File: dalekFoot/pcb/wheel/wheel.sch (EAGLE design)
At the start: 81 parts, among them IC1 LM1117MP-3.3, IC2 LM1117MP-3.3, IC3 LM1117MP-3.3, IC4 4051D, IC5 4051D, IC6 LM1117MP-3.3, U1 TB6612FNG(O,C,8,EL, U2 SS8050-SOT-23, U3 SS8050-SOT-23, U4 SS8050-SOT-23, U5 TB6612FNG(O,C,8,EL, U6 TB6612FNG(O,C,8,EL

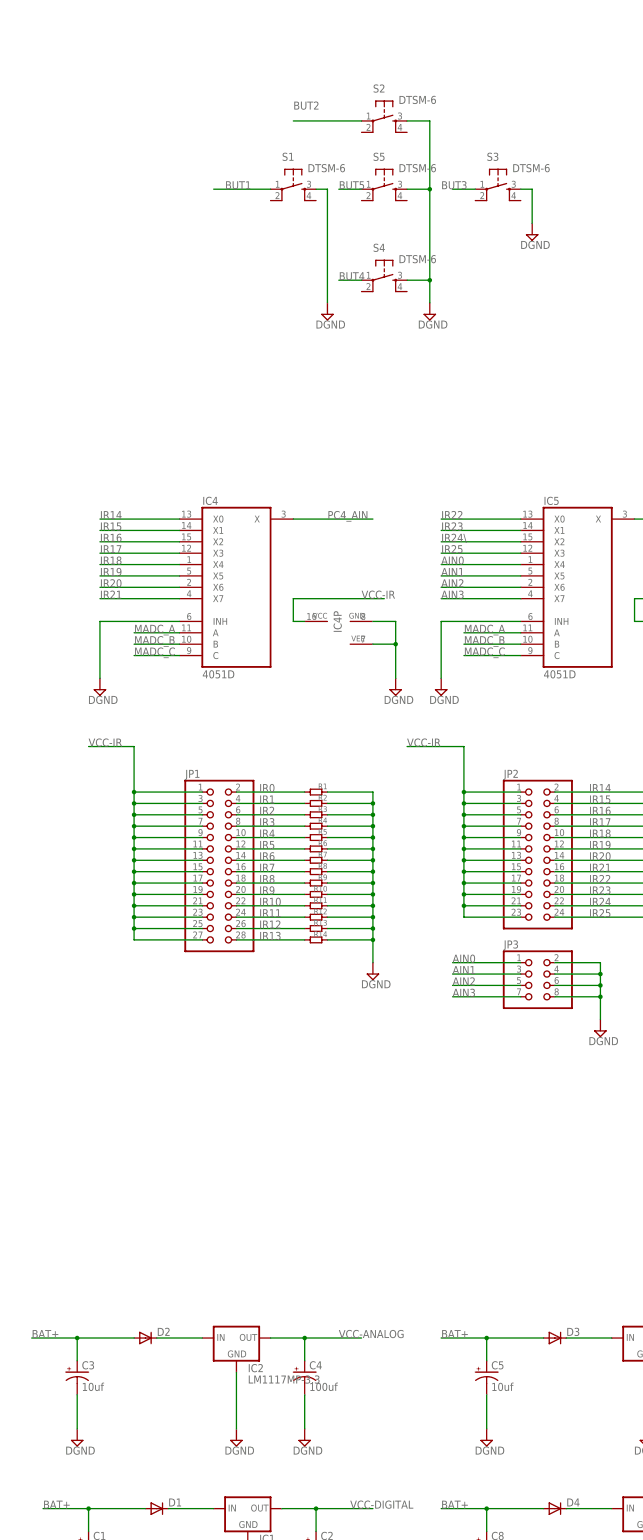
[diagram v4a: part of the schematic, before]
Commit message: 1. bugfix: fix net name typo 2. remove one unused phase power supply 3. make board more compact
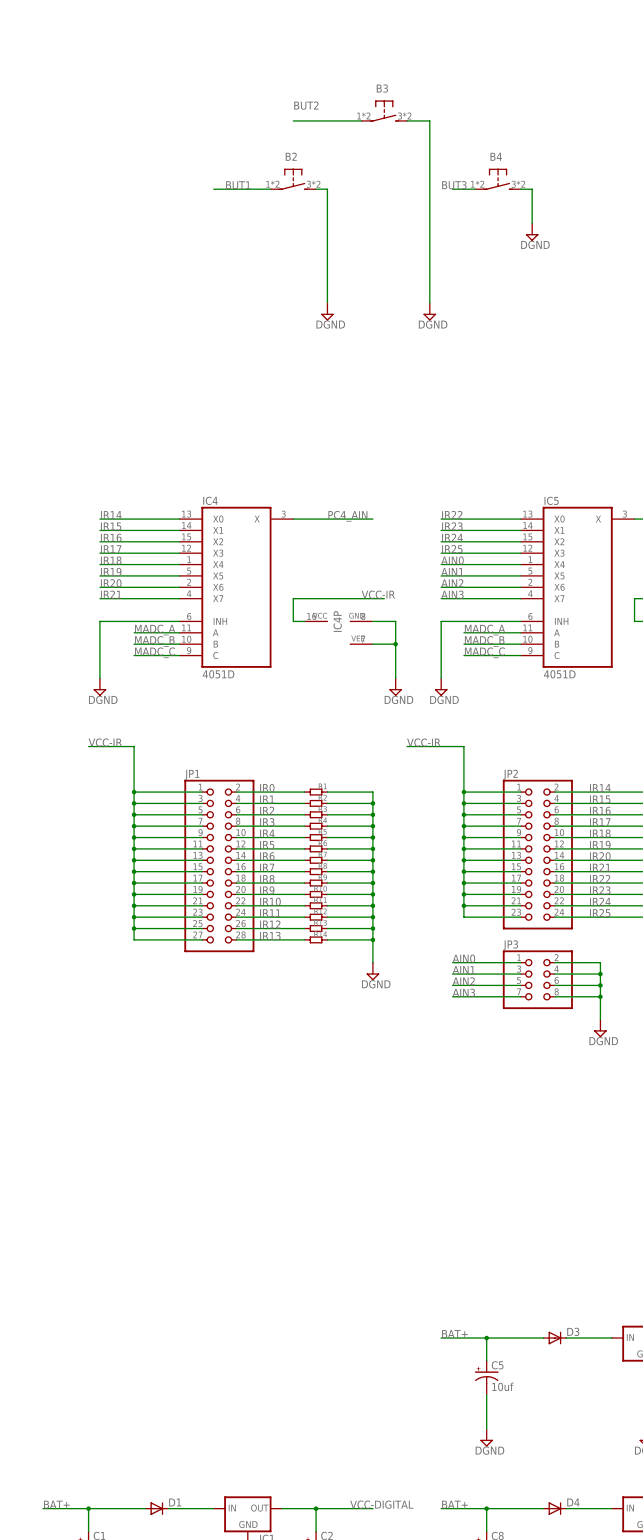
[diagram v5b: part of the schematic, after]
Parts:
- removed C3: 10uf, rcl:CPOL-US153CLV-0505
- removed C4: 100uf, rcl:CPOL-US153CLV-0605
- removed D2: (no value), diode:DIODE-DO-214AC
- removed IC2: LM1117MP-3.3, lm1117:LM1117MP-3.3
- removed S1, S2, S3, S4, S5: DTSM-6, switch-tact:DTSM-6
- added B2, B3, B4: (no value), switch-tact:DTSM-6-2PIN
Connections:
- removed net IR24\: IC5A.X2
- removed net N$1: D2.C, IC2.IN
- removed net VCC-ANALOG: C4.+, IC2.OUT
- net BAT+: no longer C3.+, D2.A
- net BUT1: now also B2.1; no longer S1.1
- net BUT2: now also B3.1; no longer S2.1
- net BUT3: now also B4.1; no longer S3.1
- net BUT4: no longer S4.1
- net BUT5: no longer S5.1
- net DGND: now also B2.2, B3.2, B4.2; no longer C3.-, C4.-, IC2.GND, S1.3, S2.3, S3.3, S4.3, S5.3
- net IR24: now also IC5A.X2
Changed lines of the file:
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@@
 <part name="SUPPLY2" library="supply2" deviceset="DGND" device=""/>
 <part name="SUPPLY3" library="supply2" deviceset="DGND" device=""/>
-<part name="IC2" library="lm1117" deviceset="LM1117?-*" device="MP" technology="3.3"/>
-<part name="SUPPLY4" library="supply2" deviceset="DGND" device=""/>
-<part name="C3" library="rcl" deviceset="CPOL-US" device="153CLV-0505" value="10uf"/>
-<part name="C4" library="rcl" deviceset="CPOL-US" device="153CLV-0605" value="100uf"/>
-<part name="SUPPLY5" library="supply2" deviceset="DGND" device=""/>
-<part name="SUPPLY6" library="supply2" deviceset="DGND" device=""/>
 <part name="U1" library="TB6612FNG" deviceset="TB6612FNG(O,C,8,EL" device=""/>
 <part name="SUPPLY7" library="supply2" deviceset="DGND" device=""/>
@@
 <part name="SUPPLY8" library="supply2" deviceset="DGND" device=""/>
 <part name="D1" library="diode" deviceset="DIODE-" device="DO-214AC"/>
-<part name="D2" library="diode" deviceset="DIODE-" device="DO-214AC"/>
 <part name="R1" library="hqc" deviceset="R-0603" device=""/>
 <part name="R2" library="hqc" deviceset="R-0603" device=""/>
@@
 <part name="SUPPLY39" library="supply2" deviceset="DGND" device=""/>
 <part name="R36" library="rcl" deviceset="R-EU_" device="R0402"/>
-<part name="S1" library="switch-tact" deviceset="DTSM-6" device=""/>
-<part name="S2" library="switch-tact" deviceset="DTSM-6" device=""/>
-<part name="S3" library="switch-tact" deviceset="DTSM-6" device=""/>
-<part name="S4" library="switch-tact" deviceset="DTSM-6" device=""/>
-<part name="S5" library="switch-tact" deviceset="DTSM-6" device=""/>
+<part name="B2" library="switch-tact" deviceset="DTSM-6-2PIN" device=""/>
+<part name="B3" library="switch-tact" deviceset="DTSM-6-2PIN" device=""/>
+<part name="B4" library="switch-tact" deviceset="DTSM-6-2PIN" device=""/>
 </parts>
 <sheets>
@@
 <instance part="SUPPLY2" gate="G$1" x="81.28" y="58.42"/>
 <instance part="SUPPLY3" gate="G$1" x="30.48" y="58.42"/>
-<instance part="IC2" gate="G$1" x="63.5" y="119.38"/>
-<instance part="SUPPLY4" gate="G$1" x="63.5" y="96.52"/>
-<instance part="C3" gate="G$1" x="27.94" y="111.76"/>
-<instance part="C4" gate="G$1" x="78.74" y="111.76"/>
-<instance part="SUPPLY5" gate="G$1" x="78.74" y="96.52"/>
-<instance part="SUPPLY6" gate="G$1" x="27.94" y="96.52"/>
 <instance part="U1" gate="G$1" x="53.34" y="596.9"/>
 <instance part="SUPPLY7" gate="G$1" x="73.66" y="558.8"/>
@@
 <instance part="SUPPLY8" gate="G$1" x="330.2" y="43.18"/>
 <instance part="D1" gate="G$1" x="45.72" y="81.28"/>
-<instance part="D2" gate="G$1" x="43.18" y="119.38"/>
 <instance part="R1" gate="G$1" x="81.28" y="241.3" rot="R180"/>
 <instance part="R2" gate="G$1" x="81.28" y="238.76" rot="R180"/>
@@
 <instance part="SUPPLY39" gate="G$1" x="325.12" y="215.9"/>
 <instance part="R36" gate="G$1" x="312.42" y="228.6"/>
-<instance part="S1" gate="G$1" x="76.2" y="375.92" rot="R270"/>
-<instance part="S2" gate="G$1" x="96.52" y="391.16" rot="R270"/>
-<instance part="S3" gate="G$1" x="121.92" y="375.92" rot="R270"/>
-<instance part="S4" gate="G$1" x="96.52" y="355.6" rot="R270"/>
-<instance part="S5" gate="G$1" x="96.52" y="375.92" rot="R270"/>
+<instance part="B2" gate="G$1" x="76.2" y="375.92" rot="R270"/>
+<instance part="B3" gate="G$1" x="96.52" y="391.16" rot="R270"/>
+<instance part="B4" gate="G$1" x="121.92" y="375.92" rot="R270"/>
 </instances>
 <busses>
@@
 <pinref part="SUPPLY2" gate="G$1" pin="DGND"/>
 <wire x1="81.28" y1="68.58" x2="81.28" y2="60.96" width="0.1524" layer="91"/>
-</segment>
-<segment>
-<pinref part="IC2" gate="G$1" pin="GND"/>
-<pinref part="SUPPLY4" gate="G$1" pin="DGND"/>
-<wire x1="63.5" y1="111.76" x2="63.5" y2="99.06" width="0.1524" layer="91"/>
-</segment>
-<segment>
-<pinref part="SUPPLY6" gate="G$1" pin="DGND"/>
-<pinref part="C3" gate="G$1" pin="-"/>
-<wire x1="27.94" y1="99.06" x2="27.94" y2="106.68" width="0.1524" layer="91"/>
-</segment>
-<segment>
-<pinref part="C4" gate="G$1" pin="-"/>
-<pinref part="SUPPLY5" gate="G$1" pin="DGND"/>
-<wire x1="78.74" y1="106.68" x2="78.74" y2="99.06" width="0.1524" layer="91"/>
 </segment>
 <segment>
@@
 </segment>
 <segment>
-<wire x1="101.6" y1="355.6" x2="106.68" y2="355.6" width="0.1524" layer="91"/>
 <pinref part="SUPPLY31" gate="G$1" pin="DGND"/>
-<wire x1="106.68" y1="355.6" x2="106.68" y2="350.52" width="0.1524" layer="91"/>
-<wire x1="101.6" y1="375.92" x2="106.68" y2="375.92" width="0.1524" layer="91"/>
-<wire x1="106.68" y1="375.92" x2="106.68" y2="355.6" width="0.1524" layer="91"/>
-<junction x="106.68" y="355.6"/>
+<wire x1="106.68" y1="391.16" x2="106.68" y2="350.52" width="0.1524" layer="91"/>
 <wire x1="101.6" y1="391.16" x2="106.68" y2="391.16" width="0.1524" layer="91"/>
-<wire x1="106.68" y1="391.16" x2="106.68" y2="375.92" width="0.1524" layer="91"/>
-<junction x="106.68" y="375.92"/>
-<pinref part="S2" gate="G$1" pin="3"/>
-<pinref part="S5" gate="G$1" pin="3"/>
-<pinref part="S4" gate="G$1" pin="3"/>
+<pinref part="B3" gate="G$1" pin="2"/>
 </segment>
 <segment>
@@
 <wire x1="83.82" y1="375.92" x2="83.82" y2="350.52" width="0.1524" layer="91"/>
 <pinref part="SUPPLY32" gate="G$1" pin="DGND"/>
-<pinref part="S1" gate="G$1" pin="3"/>
+<pinref part="B2" gate="G$1" pin="2"/>
 </segment>
 <segment>
@@
 <wire x1="129.54" y1="375.92" x2="129.54" y2="368.3" width="0.1524" layer="91"/>
 <pinref part="SUPPLY33" gate="G$1" pin="DGND"/>
-<pinref part="S3" gate="G$1" pin="3"/>
+<pinref part="B4" gate="G$1" pin="2"/>
 </segment>
 <segment>
@@
 </segment>
 <segment>
-<wire x1="17.78" y1="119.38" x2="27.94" y2="119.38" width="0.1524" layer="91"/>
-<pinref part="C3" gate="G$1" pin="+"/>
-<wire x1="27.94" y1="114.3" x2="27.94" y2="119.38" width="0.1524" layer="91"/>
-<label x="17.78" y="119.38" size="1.778" layer="95"/>
-<wire x1="27.94" y1="119.38" x2="40.64" y2="119.38" width="0.1524" layer="91"/>
-<junction x="27.94" y="119.38"/>
-<pinref part="D2" gate="G$1" pin="A"/>
-</segment>
-<segment>
 <pinref part="U1" gate="G$1" pin="VM1"/>
 <wire x1="68.58" y1="619.76" x2="73.66" y2="619.76" width="0.1524" layer="91"/>
@@
 </segment>
 </net>
-<net name="VCC-ANALOG" class="0">
-<segment>
-<pinref part="IC2" gate="G$1" pin="OUT"/>
-<wire x1="71.12" y1="119.38" x2="78.74" y2="119.38" width="0.1524" layer="91"/>
-<pinref part="C4" gate="G$1" pin="+"/>
-<wire x1="78.74" y1="119.38" x2="91.44" y2="119.38" width="0.1524" layer="91"/>
-<wire x1="78.74" y1="114.3" x2="78.74" y2="119.38" width="0.1524" layer="91"/>
-<junction x="78.74" y="119.38"/>
-<label x="86.36" y="119.38" size="1.778" layer="95"/>
-</segment>
-</net>
 <net name="AO3.1" class="0">
 <segment>
@@
 </segment>
 </net>
-<net name="N$1" class="0">
-<segment>
-<pinref part="D2" gate="G$1" pin="C"/>
-<pinref part="IC2" gate="G$1" pin="IN"/>
-<wire x1="45.72" y1="119.38" x2="55.88" y2="119.38" width="0.1524" layer="91"/>
-</segment>
-</net>
 <net name="N$5" class="0">
 <segment>
@@
 <wire x1="154.94" y1="215.9" x2="134.62" y2="215.9" width="0.1524" layer="91"/>
 <label x="142.24" y="215.9" size="1.778" layer="95"/>
+</segment>
+<segment>
+<pinref part="IC5" gate="A" pin="X2"/>
+<wire x1="127" y1="297.18" x2="109.22" y2="297.18" width="0.1524" layer="91"/>
+<label x="109.22" y="297.18" size="1.778" layer="95"/>
 </segment>
 </net>
@@
 </segment>
 </net>
-<net name="IR24\" class="0">
-<segment>
-<pinref part="IC5" gate="A" pin="X2"/>
-<wire x1="127" y1="297.18" x2="109.22" y2="297.18" width="0.1524" layer="91"/>
-<label x="109.22" y="297.18" size="1.778" layer="95"/>
-</segment>
-</net>
 <net name="MADC_A" class="0">
 <segment>
@@
 <wire x1="71.12" y1="375.92" x2="58.42" y2="375.92" width="0.1524" layer="91"/>
 <label x="60.96" y="375.92" size="1.778" layer="95"/>
-<pinref part="S1" gate="G$1" pin="1"/>
+<pinref part="B2" gate="G$1" pin="1"/>
 </segment>
 </net>
@@
 <wire x1="91.44" y1="391.16" x2="76.2" y2="391.16" width="0.1524" layer="91"/>
 <label x="76.2" y="393.7" size="1.778" layer="95"/>
-<pinref part="S2" gate="G$1" pin="1"/>
+<pinref part="B3" gate="G$1" pin="1"/>
 </segment>
 </net>
@@
 <wire x1="111.76" y1="375.92" x2="116.84" y2="375.92" width="0.1524" layer="91"/>
 <label x="109.22" y="375.92" size="1.778" layer="95"/>
-<pinref part="S3" gate="G$1" pin="1"/>
+<pinref part="B4" gate="G$1" pin="1"/>
 </segment>
 </net>
@@
 <label x="378.46" y="96.52" size="1.778" layer="95"/>
 </segment>
-<segment>
-<wire x1="86.36" y1="355.6" x2="91.44" y2="355.6" width="0.1524" layer="91"/>
-<label x="86.36" y="355.6" size="1.778" layer="95"/>
-<pinref part="S4" gate="G$1" pin="1"/>
-</segment>
 </net>
 <net name="BUT5" class="0">
@@
 <label x="378.46" y="93.98" size="1.778" layer="95"/>
 </segment>
-<segment>
-<wire x1="91.44" y1="375.92" x2="86.36" y2="375.92" width="0.1524" layer="91"/>
-<label x="86.36" y="375.92" size="1.778" layer="95"/>
-<pinref part="S5" gate="G$1" pin="1"/>
-</segment>
-</net>
+</net>

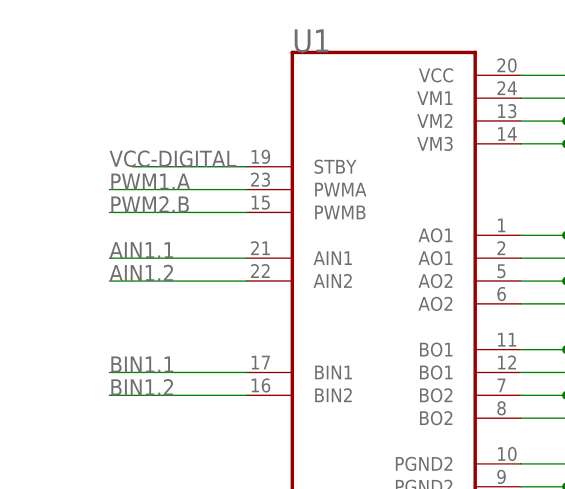
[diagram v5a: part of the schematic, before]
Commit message: modify u1 bug and IRT
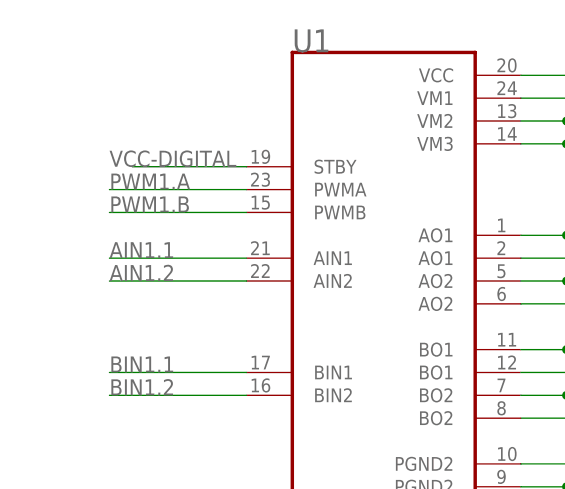
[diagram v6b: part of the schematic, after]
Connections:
- net PWM1.B: now also U1.PWMB
- net PWM2.B: no longer U1.PWMB
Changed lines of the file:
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@@
 <?xml version="1.0" encoding="utf-8"?>
 <!DOCTYPE eagle SYSTEM "eagle.dtd">
-<eagle version="7.2.0">
+<eagle version="8.2.1">
 <drawing>
 <settings>
@@
 <setting verticaltext="up"/>
 </settings>
-<grid distance="0.1" unitdist="inch" unit="mil" style="lines" multiple="1" display="yes" altdistance="0.01" altunitdist="inch" altunit="inch"/>
+<grid distance="0.1" unitdist="inch" unit="inch" style="lines" multiple="1" display="no" altdistance="0.01" altunitdist="inch" altunit="inch"/>
 <layers>
 <layer number="1" name="Top" color="4" fill="1" visible="no" active="no"/>
@@
 </segment>
 <segment>
+<pinref part="U5" gate="G$1" pin="PWMB"/>
+<wire x1="129.54" y1="607.06" x2="144.78" y2="607.06" width="0.1524" layer="91"/>
+<label x="129.54" y="607.06" size="1.778" layer="95"/>
+</segment>
+</net>
+<net name="LED1" class="0">
+<segment>
+<pinref part="U$1" gate="G$1" pin="P$C6"/>
+<wire x1="330.2" y1="88.9" x2="337.82" y2="88.9" width="0.1524" layer="91"/>
+<label x="332.74" y="88.9" size="1.778" layer="95"/>
+</segment>
+<segment>
+<pinref part="R30" gate="G$1" pin="P$1"/>
+<wire x1="83.82" y1="431.8" x2="71.12" y2="431.8" width="0.1524" layer="91"/>
+<label x="71.12" y="431.8" size="1.778" layer="95"/>
+</segment>
+</net>
+<net name="LED2" class="0">
+<segment>
+<pinref part="U$1" gate="G$1" pin="P$C7"/>
+<wire x1="330.2" y1="86.36" x2="337.82" y2="86.36" width="0.1524" layer="91"/>
+<label x="332.74" y="86.36" size="1.778" layer="95"/>
+</segment>
+<segment>
+<pinref part="R31" gate="G$1" pin="P$1"/>
+<wire x1="134.62" y1="431.8" x2="121.92" y2="431.8" width="0.1524" layer="91"/>
+<label x="124.46" y="431.8" size="1.778" layer="95"/>
+</segment>
+</net>
+<net name="PWM3.A" class="0">
+<segment>
+<pinref part="U$1" gate="G$1" pin="P$C8"/>
+<wire x1="330.2" y1="83.82" x2="337.82" y2="83.82" width="0.1524" layer="91"/>
+<label x="332.74" y="83.82" size="1.778" layer="95"/>
+</segment>
+<segment>
+<pinref part="U6" gate="G$1" pin="PWMA"/>
+<wire x1="266.7" y1="609.6" x2="251.46" y2="609.6" width="0.1524" layer="91"/>
+<label x="251.46" y="609.6" size="1.778" layer="95"/>
+</segment>
+</net>
+<net name="PWM3.B" class="0">
+<segment>
+<pinref part="U6" gate="G$1" pin="PWMB"/>
+<wire x1="251.46" y1="607.06" x2="266.7" y2="607.06" width="0.1524" layer="91"/>
+<label x="251.46" y="607.06" size="1.778" layer="95"/>
+</segment>
+<segment>
+<pinref part="U$1" gate="G$1" pin="P$A15"/>
+<wire x1="281.94" y1="66.04" x2="292.1" y2="66.04" width="0.1524" layer="91"/>
+<label x="284.48" y="66.04" size="1.778" layer="95"/>
+</segment>
+</net>
+<net name="N$9" class="0">
+<segment>
+<pinref part="R29" gate="G$1" pin="P$2"/>
+<pinref part="C7" gate="G$1" pin="P$1"/>
+<wire x1="25.4" y1="431.8" x2="30.48" y2="431.8" width="0.1524" layer="91"/>
+</segment>
+</net>
+<net name="N$12" class="0">
+<segment>
+<pinref part="C7" gate="G$1" pin="P$2"/>
+<pinref part="U2" gate="G$1" pin="P$B"/>
+<wire x1="35.56" y1="431.8" x2="40.64" y2="431.8" width="0.1524" layer="91"/>
+</segment>
+</net>
+<net name="PWM1.A" class="0">
+<segment>
+<pinref part="U$1" gate="G$1" pin="P$D12"/>
+<wire x1="353.06" y1="73.66" x2="360.68" y2="73.66" width="0.1524" layer="91"/>
+<label x="355.6" y="73.66" size="1.778" layer="95"/>
+</segment>
+<segment>
+<pinref part="U1" gate="G$1" pin="PWMA"/>
+<wire x1="38.1" y1="609.6" x2="22.86" y2="609.6" width="0.1524" layer="91"/>
+<label x="22.86" y="609.6" size="1.778" layer="95"/>
+</segment>
+</net>
+<net name="PWM1.B" class="0">
+<segment>
+<pinref part="U$1" gate="G$1" pin="P$D13"/>
+<wire x1="360.68" y1="71.12" x2="353.06" y2="71.12" width="0.1524" layer="91"/>
+<label x="355.6" y="71.12" size="1.778" layer="95"/>
+</segment>
+<segment>
 <pinref part="U1" gate="G$1" pin="PWMB"/>
 <wire x1="22.86" y1="607.06" x2="38.1" y2="607.06" width="0.1524" layer="91"/>
 <label x="22.86" y="607.06" size="1.778" layer="95"/>
 </segment>
-<segment>
-<pinref part="U5" gate="G$1" pin="PWMB"/>
-<wire x1="129.54" y1="607.06" x2="144.78" y2="607.06" width="0.1524" layer="91"/>
-<label x="129.54" y="607.06" size="1.778" layer="95"/>
-</segment>
-</net>
-<net name="LED1" class="0">
-<segment>
-<pinref part="U$1" gate="G$1" pin="P$C6"/>
-<wire x1="330.2" y1="88.9" x2="337.82" y2="88.9" width="0.1524" layer="91"/>
-<label x="332.74" y="88.9" size="1.778" layer="95"/>
-</segment>
-<segment>
-<pinref part="R30" gate="G$1" pin="P$1"/>
-<wire x1="83.82" y1="431.8" x2="71.12" y2="431.8" width="0.1524" layer="91"/>
-<label x="71.12" y="431.8" size="1.778" layer="95"/>
-</segment>
-</net>
-<net name="LED2" class="0">
-<segment>
-<pinref part="U$1" gate="G$1" pin="P$C7"/>
-<wire x1="330.2" y1="86.36" x2="337.82" y2="86.36" width="0.1524" layer="91"/>
-<label x="332.74" y="86.36" size="1.778" layer="95"/>
-</segment>
-<segment>
-<pinref part="R31" gate="G$1" pin="P$1"/>
-<wire x1="134.62" y1="431.8" x2="121.92" y2="431.8" width="0.1524" layer="91"/>
-<label x="124.46" y="431.8" size="1.778" layer="95"/>
-</segment>
-</net>
-<net name="PWM3.A" class="0">
-<segment>
-<pinref part="U$1" gate="G$1" pin="P$C8"/>
-<wire x1="330.2" y1="83.82" x2="337.82" y2="83.82" width="0.1524" layer="91"/>
-<label x="332.74" y="83.82" size="1.778" layer="95"/>
-</segment>
-<segment>
-<pinref part="U6" gate="G$1" pin="PWMA"/>
-<wire x1="266.7" y1="609.6" x2="251.46" y2="609.6" width="0.1524" layer="91"/>
-<label x="251.46" y="609.6" size="1.778" layer="95"/>
-</segment>
-</net>
-<net name="PWM3.B" class="0">
-<segment>
-<pinref part="U6" gate="G$1" pin="PWMB"/>
-<wire x1="251.46" y1="607.06" x2="266.7" y2="607.06" width="0.1524" layer="91"/>
-<label x="251.46" y="607.06" size="1.778" layer="95"/>
-</segment>
-<segment>
-<pinref part="U$1" gate="G$1" pin="P$A15"/>
-<wire x1="281.94" y1="66.04" x2="292.1" y2="66.04" width="0.1524" layer="91"/>
-<label x="284.48" y="66.04" size="1.778" layer="95"/>
-</segment>
-</net>
-<net name="N$9" class="0">
-<segment>
-<pinref part="R29" gate="G$1" pin="P$2"/>
-<pinref part="C7" gate="G$1" pin="P$1"/>
-<wire x1="25.4" y1="431.8" x2="30.48" y2="431.8" width="0.1524" layer="91"/>
-</segment>
-</net>
-<net name="N$12" class="0">
-<segment>
-<pinref part="C7" gate="G$1" pin="P$2"/>
-<pinref part="U2" gate="G$1" pin="P$B"/>
-<wire x1="35.56" y1="431.8" x2="40.64" y2="431.8" width="0.1524" layer="91"/>
-</segment>
-</net>
-<net name="PWM1.A" class="0">
-<segment>
-<pinref part="U$1" gate="G$1" pin="P$D12"/>
-<wire x1="353.06" y1="73.66" x2="360.68" y2="73.66" width="0.1524" layer="91"/>
-<label x="355.6" y="73.66" size="1.778" layer="95"/>
-</segment>
-<segment>
-<pinref part="U1" gate="G$1" pin="PWMA"/>
-<wire x1="38.1" y1="609.6" x2="22.86" y2="609.6" width="0.1524" layer="91"/>
-<label x="22.86" y="609.6" size="1.778" layer="95"/>
-</segment>
-</net>
-<net name="PWM1.B" class="0">
-<segment>
-<pinref part="U$1" gate="G$1" pin="P$D13"/>
-<wire x1="360.68" y1="71.12" x2="353.06" y2="71.12" width="0.1524" layer="91"/>
-<label x="355.6" y="71.12" size="1.778" layer="95"/>
-</segment>
-</net>
+</net>
